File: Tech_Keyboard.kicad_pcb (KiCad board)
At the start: 2 copper layers, 82 x 119 mm, 39 parts, among them SW2 RotaryEncoder, U1 MCU_Seeed_XIAO_RP2040

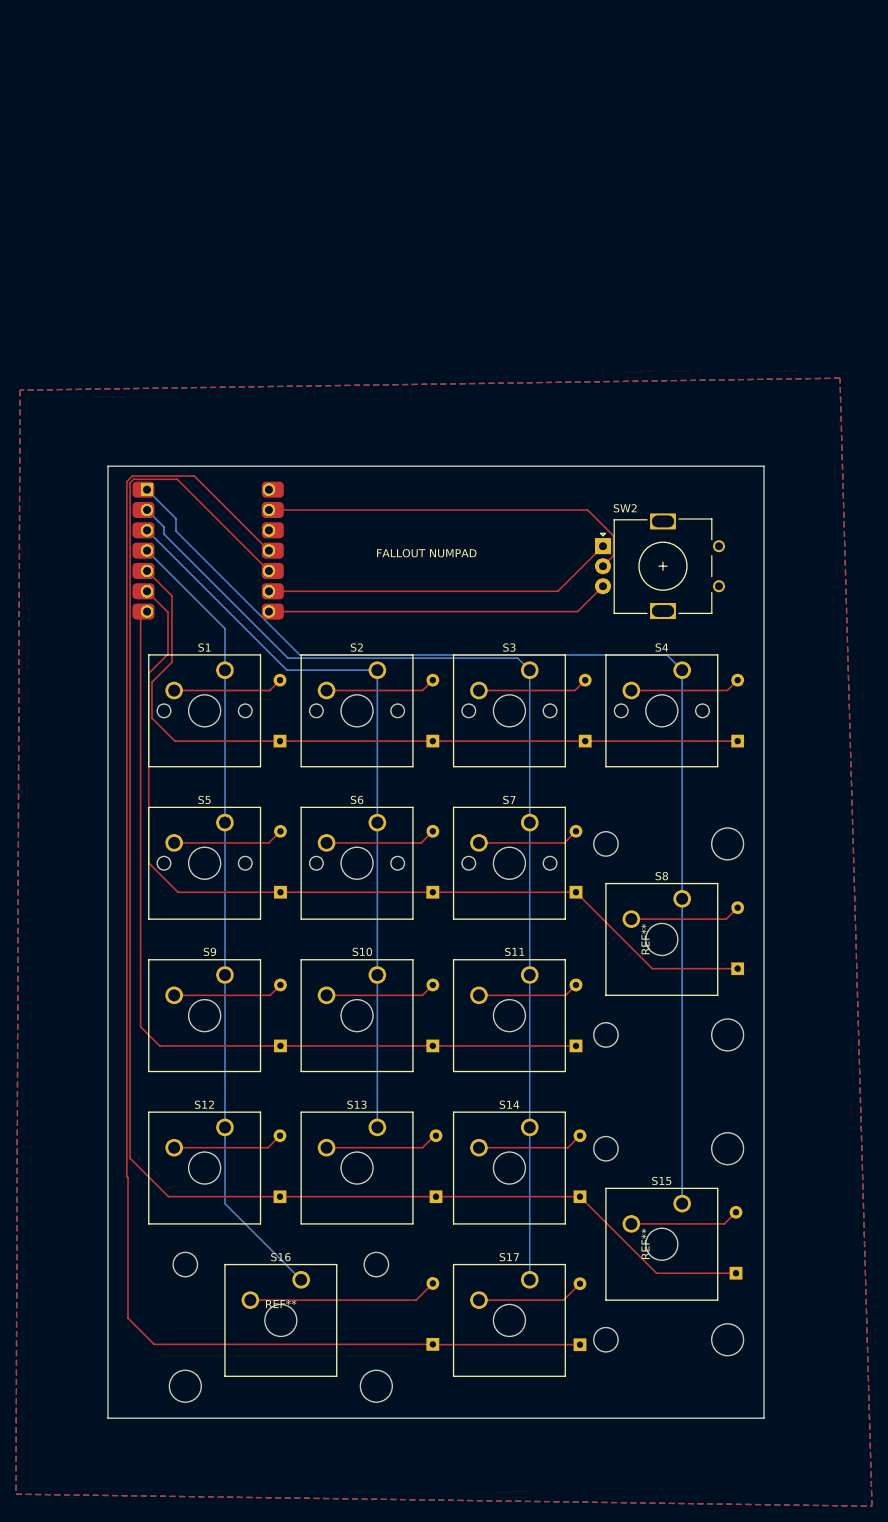
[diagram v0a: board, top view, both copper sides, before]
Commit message: updated to fish shape
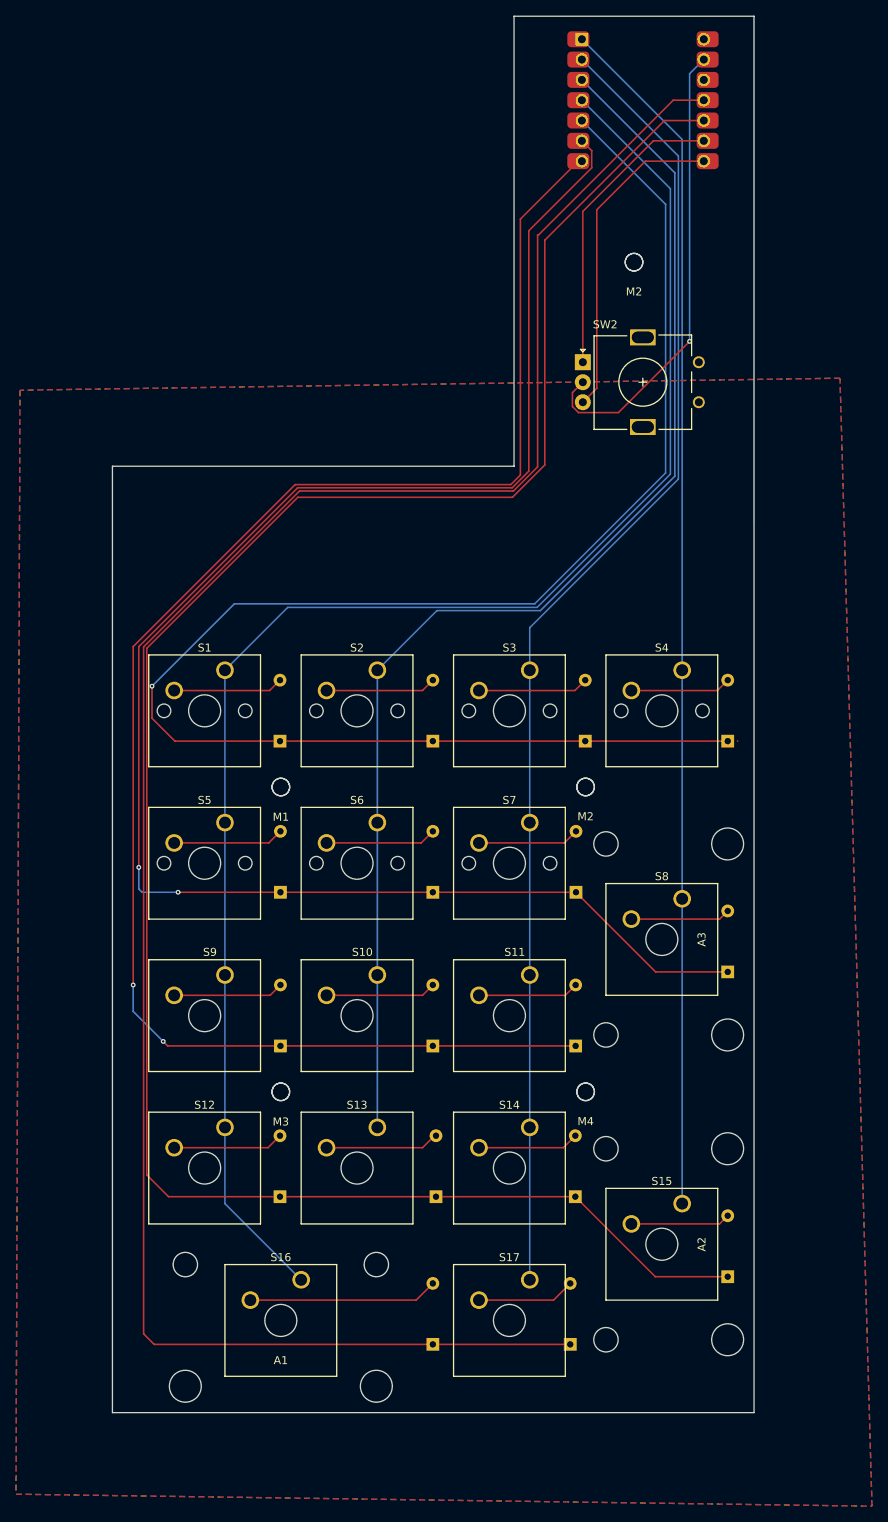
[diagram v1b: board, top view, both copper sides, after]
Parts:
- added M1: MountingHole_2.2mm_M2, MountingHole:MountingHole_2.2mm_M2, F.Cu at (132.6, 78.6)
- added M2: MountingHole_2.2mm_M2, MountingHole:MountingHole_2.2mm_M2, F.Cu at (176.8, 13.0)
- added M2: MountingHole_2.2mm_M2, MountingHole:MountingHole_2.2mm_M2, F.Cu at (170.7, 78.6)
- added M3: MountingHole_2.2mm_M2, MountingHole:MountingHole_2.2mm_M2, F.Cu at (132.6, 116.7)
- added M3: Standoff_M2x4mm, ScottoKeebs_Scotto:Standoff_M2x4mm, F.Cu at (132.6, 116.7)
- added M4: MountingHole_2.2mm_M2, MountingHole:MountingHole_2.2mm_M2, F.Cu at (170.7, 116.7)
- added REF**: Standoff_M2x4mm, ScottoKeebs_Scotto:Standoff_M2x4mm, F.Cu at (176.8, 13.0)
- added REF**: Standoff_M2x4mm, ScottoKeebs_Scotto:Standoff_M2x4mm, F.Cu at (132.6, 78.6)
- added REF**: Standoff_M2x4mm, ScottoKeebs_Scotto:Standoff_M2x4mm, F.Cu at (170.7, 116.7)
- added REF**: Standoff_M2x4mm, ScottoKeebs_Scotto:Standoff_M2x4mm, F.Cu at (170.7, 78.6)
- moved U1 78.3 mm to (177.9, -7.25)
- moved SW2 23.1 mm to (170.4, 25.5)
- moved D8 1.31 mm to (188.5, 101.7)
- moved D4 1.24 mm to (188.5, 72.9)
- moved D17 1.22 mm to (168.8, 148.3)
- moved D15 1.12 mm to (188.5, 139.8)
- moved D14 0.59 mm to (169.4, 129.8)
- renumbered REF** to A1, REF** to A2, REF** to A3
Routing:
- net Row 0: track 95.2 -> 200.8 mm, vias 0 -> 1
- net Column 0: track 99.1 -> 197.3 mm
- net Row 1: track 115.3 -> 211.3 mm, vias 0 -> 2
- net Row 2: track 107.6 -> 202.2 mm, vias 0 -> 2
- net Row 4: track 184.4 -> 255.3 mm
- net Row 3: track 188.4 -> 257.6 mm
- net Column 1: track 93.2 -> 158.7 mm
- net Column 2: track 132.9 -> 165.2 mm
- net GND: track 48.3 -> 58.2 mm, vias 0 -> 1
- net Column 3: track 143.8 -> 150.7 mm
- net R0: track 44.1 -> 37.6 mm
- net R1: track 43.1 -> 40.7 mm
- net Net-(D4-A): track 13.8 -> 12.6 mm
- net Net-(D17-A): track 13.5 -> 12.3 mm
- net Net-(D14-A): track 13.3 -> 12.7 mm
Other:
- board size 82 x 119 mm -> 80.2 x 174.6 mm
- board text removed: "FALLOUT NUMPAD"
